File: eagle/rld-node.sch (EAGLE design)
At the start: 11 parts

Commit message: Added synched layout
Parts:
- added C10, C7, C8: 100nF, rcl:C-EUC0805
- added C11: 4.7uF, rcl:C-EUC0805
- added C12: 10nF, rcl:C-EUC0805
- added C13: 1uF, rcl:C-EUC0805
- added C9: 4.7 uF, rcl:C-EUC0805
- added JP1: (no value), pinhead:PINHD-1X4
- added U$3, U$4, U$8: IHLP-1212, inductor-vishay:IHLP-1212
- added U$5: STM32-F042X4/6-48, st-microelectronics:STM32-F042X4/6-48
- added U$6, U$7: RA-02, ai-thinker:RA-02
- added X2: (no value), con-berg:PN87520
- X1: device con-wago-500:W237-102 -> con-molex:KK-156-2
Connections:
- new net N$5: U$1.SW, U$3.1
- new net N$6: U$2.SW, U$4.1
- new net SPI1_MISO: U$5.PA6
- new net SPI1_MOSI: U$5.PA7
- new net SPI1_SCK: U$5.PA5
- new net SPI2_MISO: U$5.PB14
- new net SPI2_MOSI: U$5.PB15
- new net SPI2_SCK: U$5.PB10
- new net SWCLK: JP1.3, U$5.PA14
- new net SWDIO: JP1.2, U$5.PA13
- new net USB_D+: U$5.PA12
- new net USB_D-: U$5.PA11
- net +3V3: now also C10.2, C11.2, C12.2, C13.2, C7.2, C8.2, C9.2, JP1.4, U$4.2, U$5.VDD, U$5.VDDA
- net +5V: now also U$3.2, X2.1
- net GND: now also C10.1, C11.1, C12.1, C13.1, C7.1, C8.1, C9.1, JP1.1, U$5.VSS, U$5.VSSA, X1-1.S, X2.4; no longer X1-2.KL
- net VCC: now also X1-2.S; no longer X1-1.KL

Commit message: Nearly finished design
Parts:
- removed U$8: IHLP-1212, inductor-vishay:IHLP-1212
- removed X2: (no value), con-berg:PN87520
- added C14, C15: (no value), rcl:C-EUC0805
- added C16, C17: 22 µF, Eagle_WCAP-ASLI_rev20a:WCAP-ASLI_4X5.5_865080340003
- added JP2: (no value), pinhead:PINHD-1X2
- added X3: (no value), con-wago-500:W237-102
- X1: device con-molex:KK-156-2 -> con-wago-500:W237-102
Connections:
- removed net SPI1_MISO: U$5.PA6
- removed net SPI1_MOSI: U$5.PA7
- removed net SPI1_SCK: U$5.PA5
- removed net SPI2_MISO: U$5.PB14
- removed net SPI2_MOSI: U$5.PB15
- removed net SPI2_SCK: U$5.PB10
- new net LORA1_D0: U$5.PA3, U$6.DIO0
- new net LORA1_MISO: U$5.PA6, U$6.MISO
- new net LORA1_MOSI: U$5.PA7, U$6.MOSI
- new net LORA1_NSS: U$5.PA4, U$6.NSS
- new net LORA1_RST: U$5.PA2, U$6.RESET
- new net LORA1_SCK: U$5.PA5, U$6.SCK
- new net LORA2_D0: U$5.PB12, U$7.DIO0
- new net LORA2_MISO: U$5.PB14, U$7.MISO
- new net LORA2_MOSI: U$5.PB15, U$7.MOSI
- new net LORA2_NSS: U$5.PB13, U$7.NSS
- new net LORA2_RST: U$5.PB11, U$7.RESET
- new net LORA2_SCK: U$5.PB10, U$7.SCK
- new net USART1_RX: JP2.1, U$5.PA10
- new net USART1_TX: JP2.2, U$5.PA9
- net +3V3: now also C14.2, C15.2, C16.+, C17.+, U$6.VDD, U$7.VDD
- net +5V: now also X3-1.KL; no longer X2.1
- net GND: now also C14.1, C15.1, C16.-, C17.-, U$6.VSS, U$7.VSS, X1-2.KL, X3-2.KL; no longer X1-1.S, X2.4
- net VCC: now also X1-1.KL; no longer X1-2.S
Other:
- moved on the sheet: X1-1, X1-2

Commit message: WIP
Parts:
- removed C15: (no value), rcl:C-EUC0805
- removed C17: 22 µF, Eagle_WCAP-ASLI_rev20a:WCAP-ASLI_4X5.5_865080340003
- removed X3: (no value), con-wago-500:W237-102
- added H1, H2: MOUNT-PAD-ROUND2.8, holes:MOUNT-PAD-ROUND2.8
- added X2: (no value), con-yamaichi:USB-A003
- renumbered JP1 to SYS, U$1 to L1, U$2 to L2
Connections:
- net +3V3: no longer C15.2, C17.+
- net +5V: now also X2.1; no longer X3-1.KL
- net GND: now also H1.MOUNT, H2.MOUNT, X2.4; no longer C15.1, C17.-, X3-2.KL

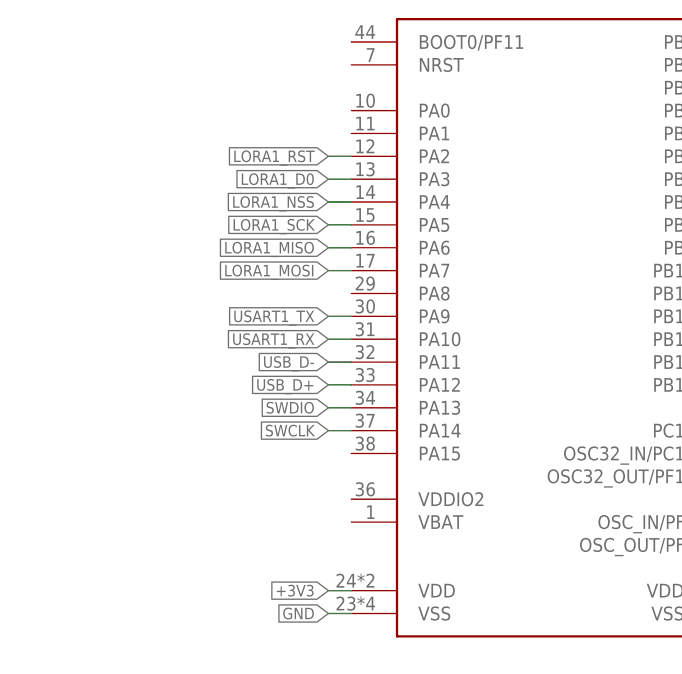
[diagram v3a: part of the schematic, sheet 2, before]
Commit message: Fixed missing voltage trace and fixed floating BOOT and NRST
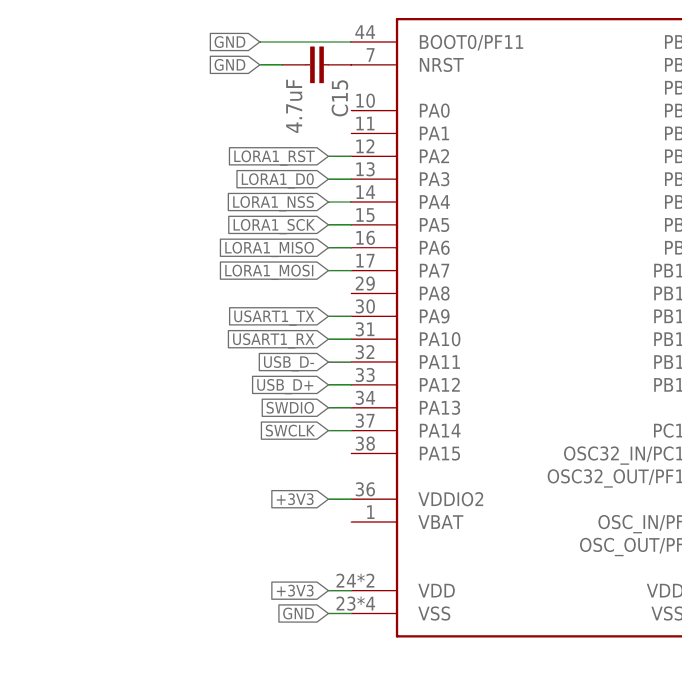
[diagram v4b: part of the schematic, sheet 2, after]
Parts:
- added C15: 4.7uF, rcl:C-EUC0805
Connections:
- new net N$8: C15.1, U$5.NRST
- net +3V3: now also U$5.VDDIO2
- net GND: now also C15.2, U$5.BOOT0/PF11
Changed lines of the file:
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@@
 <part name="GND17" library="supply1" library_urn="urn:adsk.eagle:library:371" deviceset="GND" device=""/>
 <part name="GND18" library="supply1" library_urn="urn:adsk.eagle:library:371" deviceset="GND" device=""/>
+<part name="C15" library="rcl" library_urn="urn:adsk.eagle:library:334" deviceset="C-EU" device="C0805" package3d_urn="urn:adsk.eagle:package:23617/2" value="4.7uF"/>
 </parts>
 <sheets>
@@
 <attribute name="VALUE" x="19.05" y="50.8" size="1.778" layer="96" rot="R180"/>
 </instance>
+<instance part="C15" gate="G$1" x="45.72" y="116.84" smashed="yes" rot="R270">
+<attribute name="NAME" x="46.101" y="115.316" size="1.778" layer="95" rot="R270"/>
+<attribute name="VALUE" x="41.021" y="115.316" size="1.778" layer="96" rot="R270"/>
+</instance>
 </instances>
 <busses>
@@
 <wire x1="20.32" y1="22.86" x2="20.32" y2="20.32" width="0.1524" layer="91"/>
 </segment>
+<segment>
+<pinref part="U$5" gate="G$1" pin="BOOT0/PF11"/>
+<wire x1="48.26" y1="119.38" x2="38.1" y2="119.38" width="0.1524" layer="91"/>
+<label x="38.1" y="119.38" size="1.27" layer="95" rot="R180" xref="yes"/>
+</segment>
+<segment>
+<pinref part="C15" gate="G$1" pin="2"/>
+<wire x1="40.64" y1="116.84" x2="38.1" y2="116.84" width="0.1524" layer="91"/>
+<label x="38.1" y="116.84" size="1.27" layer="95" rot="R180" xref="yes"/>
+</segment>
 </net>
 <net name="+3V3" class="0">
@@
 <wire x1="20.32" y1="30.48" x2="20.32" y2="33.02" width="0.1524" layer="91"/>
 </segment>
+<segment>
+<pinref part="U$5" gate="G$1" pin="VDDIO2"/>
+<wire x1="48.26" y1="68.58" x2="45.72" y2="68.58" width="0.1524" layer="91"/>
+<label x="45.72" y="68.58" size="1.27" layer="95" rot="R180" xref="yes"/>
+</segment>
 </net>
 <net name="SWCLK" class="0">
@@
 <wire x1="48.26" y1="101.6" x2="45.72" y2="101.6" width="0.1524" layer="91"/>
 <label x="45.72" y="101.6" size="1.27" layer="95" rot="R180" xref="yes"/>
+</segment>
+</net>
+<net name="N$8" class="0">
+<segment>
+<pinref part="U$5" gate="G$1" pin="NRST"/>
+<pinref part="C15" gate="G$1" pin="1"/>
 </segment>
 </net>
@@
 <segment>
 <pinref part="U$7" gate="G$1" pin="VDD"/>
-<wire x1="121.92" y1="93.98" x2="116.84" y2="93.98" width="0.1524" layer="91"/>
-<wire x1="116.84" y1="93.98" x2="116.84" y2="91.44" width="0.1524" layer="91"/>
-<wire x1="116.84" y1="93.98" x2="109.22" y2="93.98" width="0.1524" layer="91"/>
-<wire x1="109.22" y1="93.98" x2="109.22" y2="91.44" width="0.1524" layer="91"/>
-<junction x="116.84" y="93.98"/>
+<wire x1="121.92" y1="93.98" x2="101.6" y2="93.98" width="0.1524" layer="91"/>
 <pinref part="+3V7" gate="G$1" pin="+3V3"/>
-<wire x1="109.22" y1="93.98" x2="101.6" y2="93.98" width="0.1524" layer="91"/>
-<junction x="109.22" y="93.98"/>
 </segment>
 </net>
@@
 <pinref part="U$7" gate="G$1" pin="VSS"/>
 <wire x1="121.92" y1="91.44" x2="121.92" y2="81.28" width="0.1524" layer="91"/>
-<wire x1="121.92" y1="81.28" x2="116.84" y2="81.28" width="0.1524" layer="91"/>
-<wire x1="116.84" y1="81.28" x2="116.84" y2="83.82" width="0.1524" layer="91"/>
-<wire x1="116.84" y1="81.28" x2="109.22" y2="81.28" width="0.1524" layer="91"/>
-<wire x1="109.22" y1="81.28" x2="109.22" y2="83.82" width="0.1524" layer="91"/>
-<junction x="116.84" y="81.28"/>
 <pinref part="GND16" gate="1" pin="GND"/>
-<junction x="121.92" y="81.28"/>
-</segment>
-</net>
+</segment>
+</net>

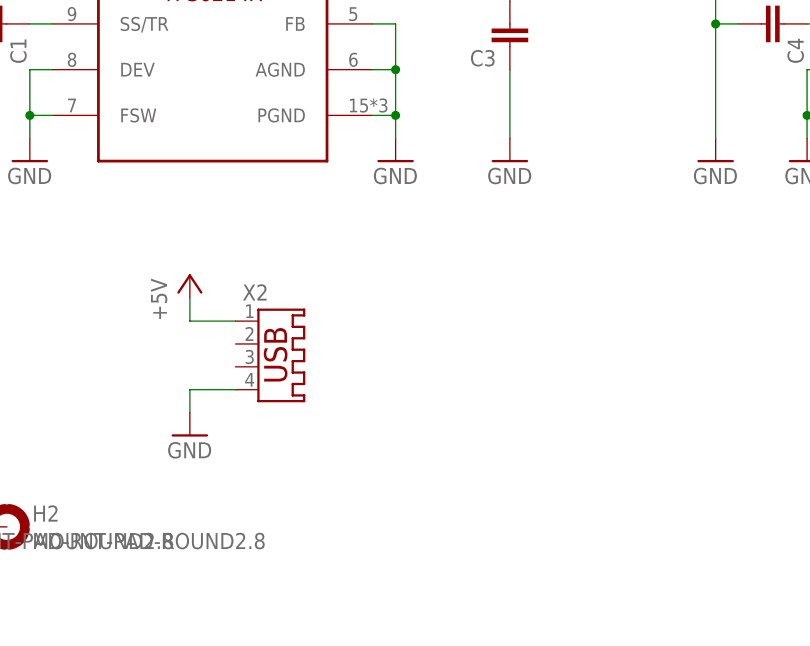
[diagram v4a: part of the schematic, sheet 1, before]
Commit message: Changed USB socket and added power LED
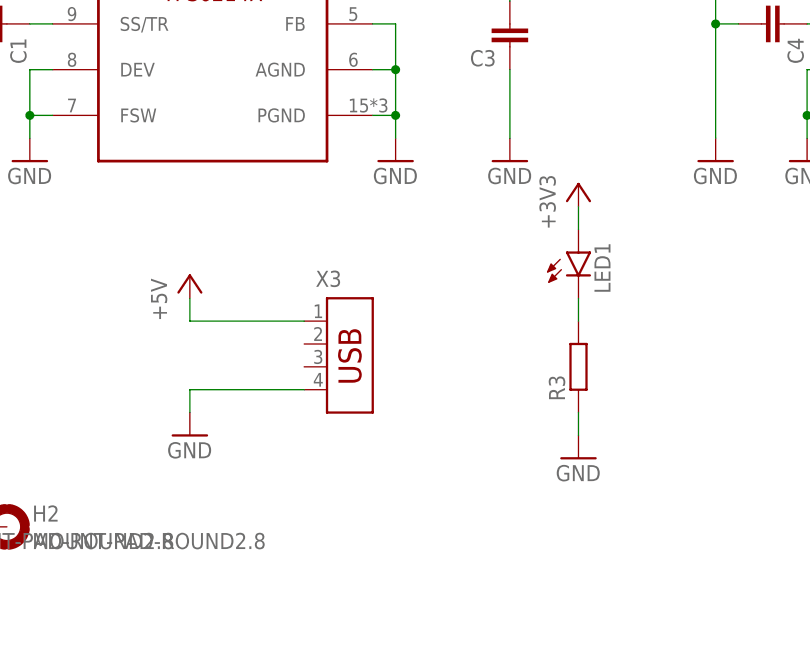
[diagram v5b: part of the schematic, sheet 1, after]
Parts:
- removed X2: (no value), con-yamaichi:USB-A003
- added LED1: (no value), led:LEDSML0805
- added R3: (no value), rcl:R-EU_R0805
- added X3: (no value), con-amp:USB-787616
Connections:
- new net N$7: LED1.C, R3.2
- net +3V3: now also LED1.A
- net +5V: now also X3.1; no longer X2.1
- net GND: now also R3.1, X3.4; no longer X2.4
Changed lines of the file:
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@@
 <part name="GND16" library="supply1" library_urn="urn:adsk.eagle:library:371" deviceset="GND" device=""/>
 <part name="+3V7" library="supply1" library_urn="urn:adsk.eagle:library:371" deviceset="+3V3" device=""/>
-<part name="X2" library="con-yamaichi" library_urn="urn:adsk.eagle:library:202" deviceset="USB-A003" device="" package3d_urn="urn:adsk.eagle:package:11805/1"/>
 <part name="H1" library="holes" library_urn="urn:adsk.eagle:library:237" deviceset="MOUNT-PAD-ROUND" device="2.8" package3d_urn="urn:adsk.eagle:package:14281/1"/>
 <part name="H2" library="holes" library_urn="urn:adsk.eagle:library:237" deviceset="MOUNT-PAD-ROUND" device="2.8" package3d_urn="urn:adsk.eagle:package:14281/1"/>
@@
 <part name="GND18" library="supply1" library_urn="urn:adsk.eagle:library:371" deviceset="GND" device=""/>
 <part name="C15" library="rcl" library_urn="urn:adsk.eagle:library:334" deviceset="C-EU" device="C0805" package3d_urn="urn:adsk.eagle:package:23617/2" value="4.7uF"/>
+<part name="X3" library="con-amp" library_urn="urn:adsk.eagle:library:127" deviceset="USB-787616" device="" package3d_urn="urn:adsk.eagle:package:8081650/1"/>
+<part name="LED1" library="led" library_urn="urn:adsk.eagle:library:259" deviceset="LED" device="SML0805" package3d_urn="urn:adsk.eagle:package:15830/1"/>
+<part name="GND19" library="supply1" library_urn="urn:adsk.eagle:library:371" deviceset="GND" device=""/>
+<part name="+3V8" library="supply1" library_urn="urn:adsk.eagle:library:371" deviceset="+3V3" device=""/>
+<part name="R3" library="rcl" library_urn="urn:adsk.eagle:library:334" deviceset="R-EU_" device="R0805" package3d_urn="urn:adsk.eagle:package:23553/2"/>
 </parts>
 <sheets>
@@
 <attribute name="NAME" x="10.16" y="61.849" size="1.778" layer="95" rot="R180"/>
 </instance>
-<instance part="X2" gate="G$1" x="55.88" y="60.96" smashed="yes">
-<attribute name="NAME" x="51.562" y="68.326" size="1.778" layer="95" ratio="10"/>
-<attribute name="VALUE" x="51.562" y="54.356" size="1.778" layer="96" ratio="10"/>
-</instance>
 <instance part="H1" gate="G$1" x="15.24" y="43.18" smashed="yes">
 <attribute name="NAME" x="18.034" y="43.7642" size="1.778" layer="95"/>
@@
 <instance part="GND18" gate="1" x="20.32" y="35.56" smashed="yes">
 <attribute name="VALUE" x="17.78" y="33.02" size="1.778" layer="96"/>
+</instance>
+<instance part="X3" gate="G$1" x="63.5" y="60.96" smashed="yes">
+<attribute name="NAME" x="59.69" y="69.85" size="1.778" layer="95"/>
+<attribute name="VALUE" x="59.69" y="53.34" size="1.778" layer="96"/>
+</instance>
+<instance part="LED1" gate="G$1" x="88.9" y="73.66" smashed="yes">
+<attribute name="NAME" x="92.456" y="69.088" size="1.778" layer="95" rot="R90"/>
+<attribute name="VALUE" x="94.615" y="69.088" size="1.778" layer="96" rot="R90"/>
+</instance>
+<instance part="GND19" gate="1" x="88.9" y="50.8" smashed="yes">
+<attribute name="VALUE" x="86.36" y="48.26" size="1.778" layer="96"/>
+</instance>
+<instance part="+3V8" gate="G$1" x="88.9" y="81.28" smashed="yes">
+<attribute name="VALUE" x="86.36" y="76.2" size="1.778" layer="96" rot="R90"/>
+</instance>
+<instance part="R3" gate="G$1" x="88.9" y="60.96" smashed="yes" rot="R90">
+<attribute name="NAME" x="87.4014" y="57.15" size="1.778" layer="95" rot="R90"/>
+<attribute name="VALUE" x="92.202" y="57.15" size="1.778" layer="96" rot="R90"/>
 </instance>
 </instances>
@@
 <pinref part="GND15" gate="1" pin="GND"/>
 <wire x1="45.72" y1="55.88" x2="45.72" y2="58.42" width="0.1524" layer="91"/>
-<wire x1="45.72" y1="58.42" x2="50.8" y2="58.42" width="0.1524" layer="91"/>
-<pinref part="X2" gate="G$1" pin="4"/>
+<pinref part="X3" gate="G$1" pin="4"/>
+<wire x1="45.72" y1="58.42" x2="58.42" y2="58.42" width="0.1524" layer="91"/>
 </segment>
 <segment>
@@
 <wire x1="20.32" y1="38.1" x2="20.32" y2="43.18" width="0.1524" layer="91"/>
 <wire x1="20.32" y1="43.18" x2="22.86" y2="43.18" width="0.1524" layer="91"/>
+</segment>
+<segment>
+<pinref part="GND19" gate="1" pin="GND"/>
+<pinref part="R3" gate="G$1" pin="1"/>
+<wire x1="88.9" y1="53.34" x2="88.9" y2="55.88" width="0.1524" layer="91"/>
 </segment>
 </net>
@@
 <pinref part="P+6" gate="1" pin="+5V"/>
 <wire x1="45.72" y1="66.04" x2="45.72" y2="68.58" width="0.1524" layer="91"/>
-<wire x1="50.8" y1="66.04" x2="45.72" y2="66.04" width="0.1524" layer="91"/>
-<pinref part="X2" gate="G$1" pin="1"/>
+<pinref part="X3" gate="G$1" pin="1"/>
+<wire x1="45.72" y1="66.04" x2="58.42" y2="66.04" width="0.1524" layer="91"/>
 </segment>
 </net>
@@
 <pinref part="U$4" gate="G$1" pin="2"/>
 </segment>
+<segment>
+<pinref part="LED1" gate="G$1" pin="A"/>
+<pinref part="+3V8" gate="G$1" pin="+3V3"/>
+<wire x1="88.9" y1="78.74" x2="88.9" y2="76.2" width="0.1524" layer="91"/>
+</segment>
 </net>
 <net name="N$5" class="0">
@@
 </segment>
 </net>
+<net name="N$7" class="0">
+<segment>
+<pinref part="R3" gate="G$1" pin="2"/>
+<pinref part="LED1" gate="G$1" pin="C"/>
+<wire x1="88.9" y1="66.04" x2="88.9" y2="68.58" width="0.1524" layer="91"/>
+</segment>
+</net>
